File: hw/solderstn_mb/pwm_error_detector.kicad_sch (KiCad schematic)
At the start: 14 parts, among them Q1701 DMG1013T, U1601 NE556d, U1701 74LVC1G175dck, U1702 74LVC1G11dck

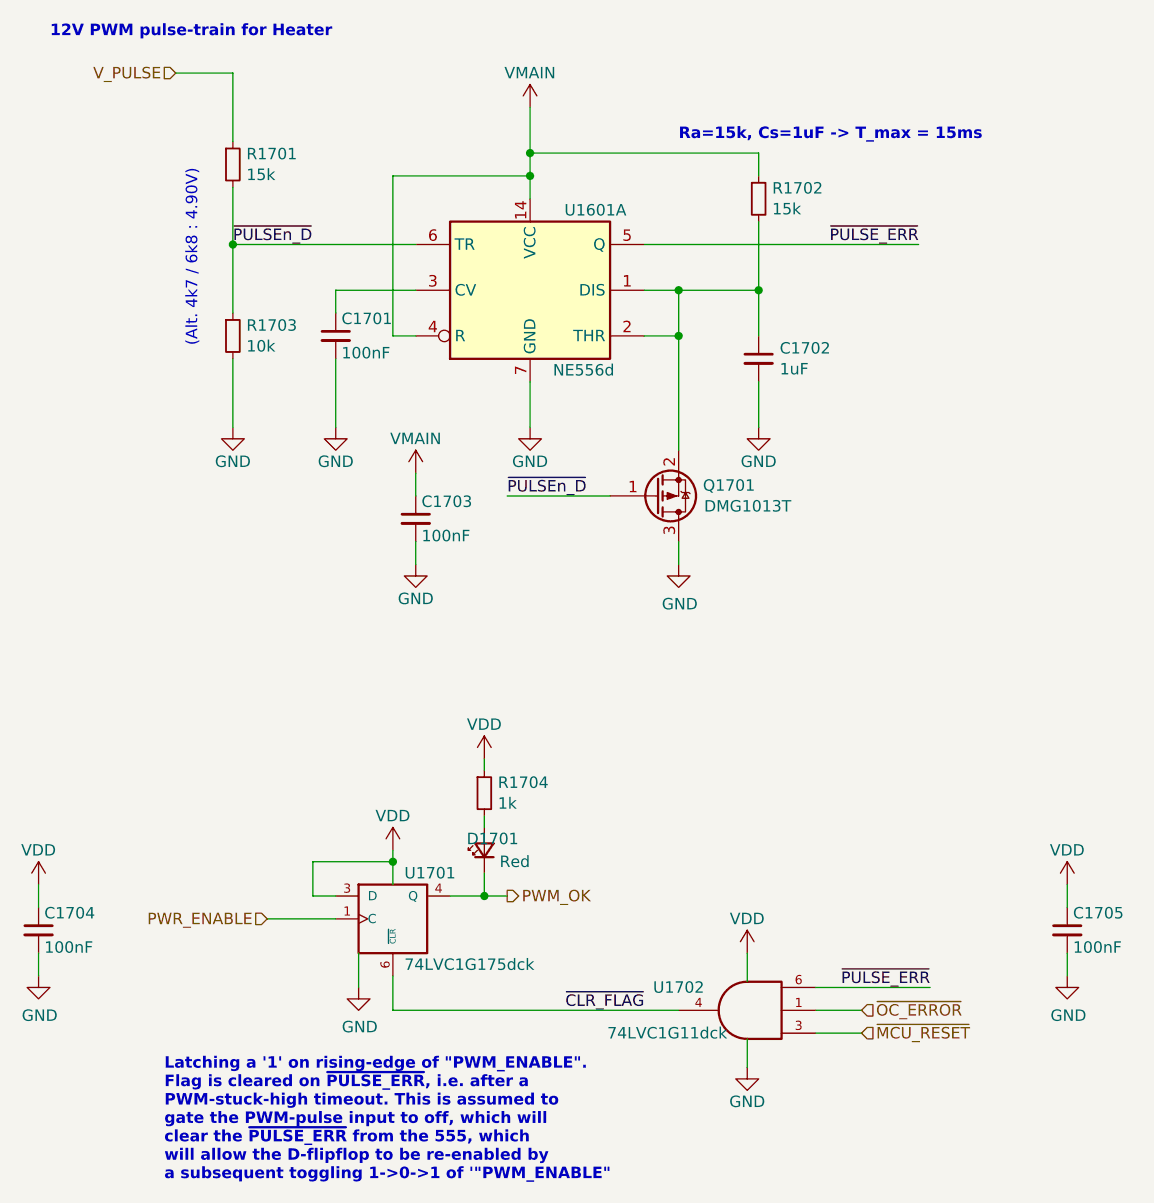
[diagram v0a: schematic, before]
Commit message: solderstn_mb::power - changed generic 2x2 connector to customlib_mj:Molex_MicroFit 2x2
(and a whole bunch of other automatic changes, crap)
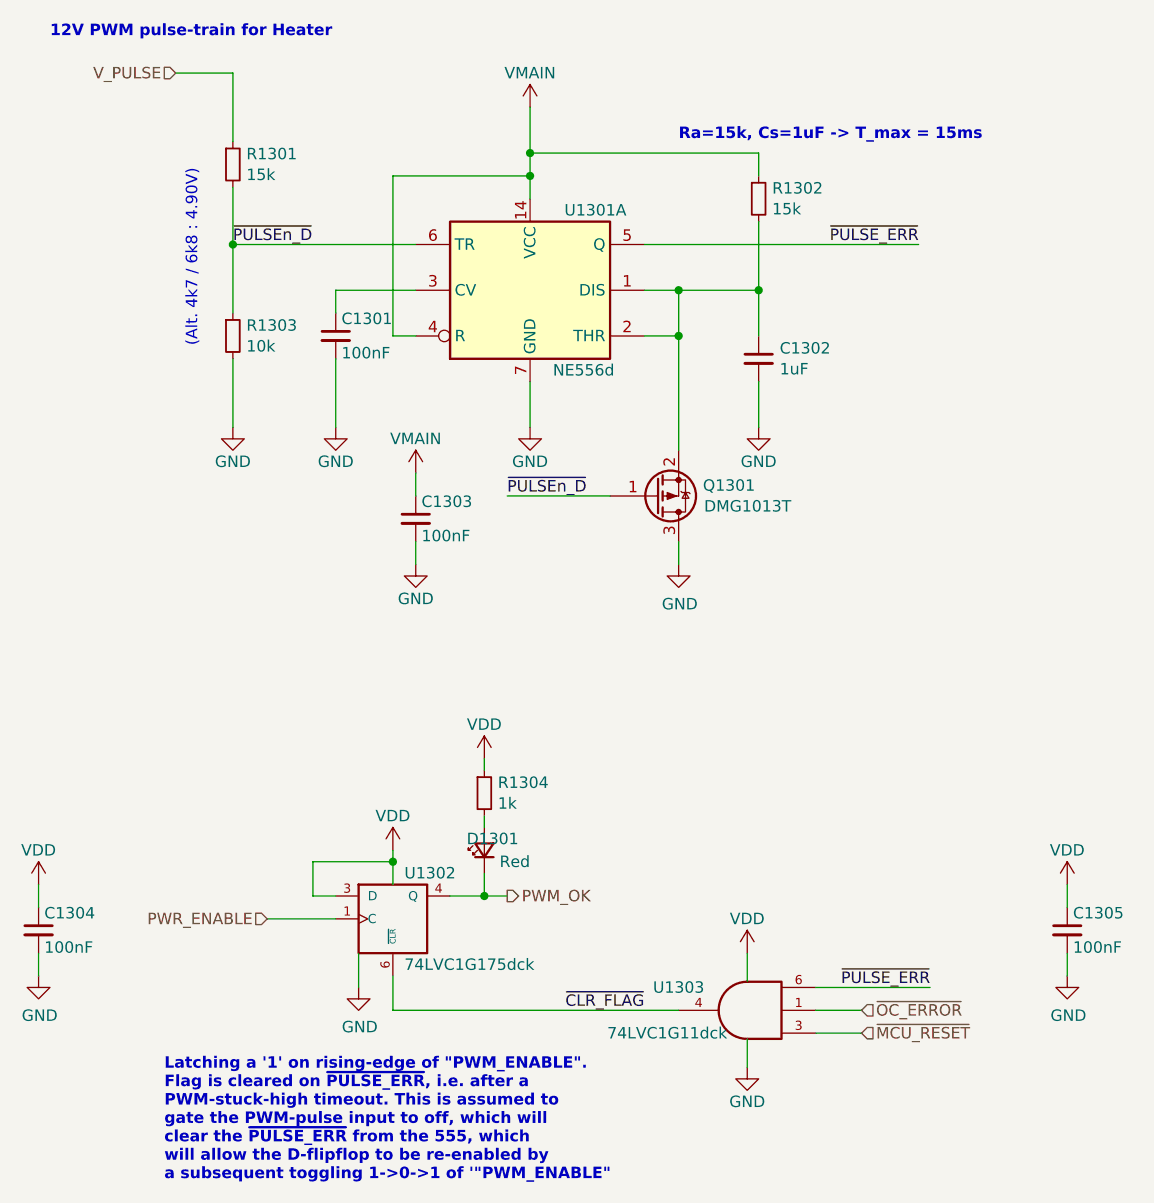
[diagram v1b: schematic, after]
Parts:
- renumbered C1701 to C1301, C1702 to C1302, C1703 to C1303, C1704 to C1304, C1705 to C1305, D1701 to D1301, Q1701 to Q1301, R1701 to R1301, R1702 to R1302, R1703 to R1303, R1704 to R1304, U1601 to U1301, U1701 to U1302, U1702 to U1303

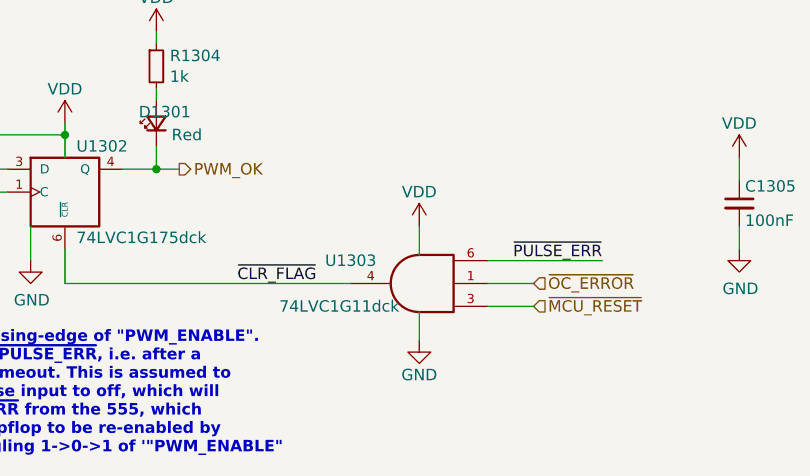
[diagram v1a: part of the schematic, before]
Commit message: hw: long-standing uncommitted stuff; mostly auto-updates (v7) fw: remove L052 tree (CMSIS & std-HAL shouldn't be committed and it was the wrong device name anyway)
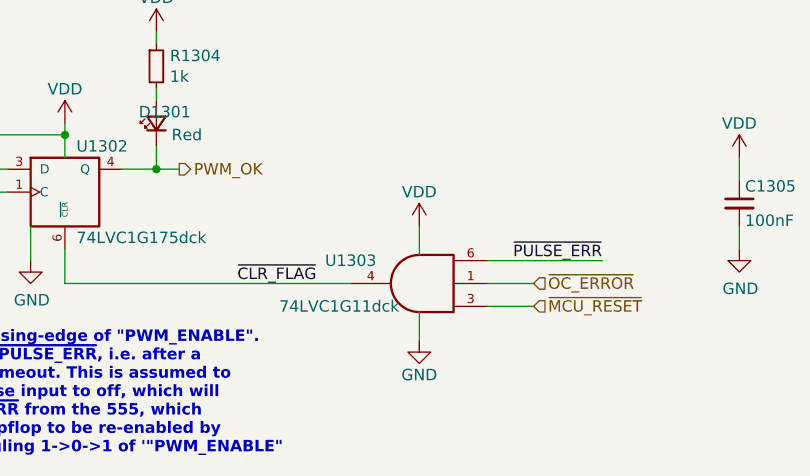
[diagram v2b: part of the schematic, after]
